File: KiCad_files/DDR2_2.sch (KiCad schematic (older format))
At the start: 16 parts, among them J6 EDY4016A

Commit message: Cleanup + Update to KiCad 5.0 + DDR2
Updated to KiCad 5, which re-organized libraries, so corrected them to not need RASAC-rescue.lib.
Also cleaned up some stuff.
DDR4 has been removed and in place will be DDR2.
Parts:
- removed J6: EDY4016A, symbol EDY4016A
- C101, C102, C103, C104, C105, C106, C107, C108, C109, C110, C111, C112: symbol C_Small -> Device:C_Small
- R29, R30: symbol R -> Device:R
- R31: symbol R_Small -> Device:R_Small
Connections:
- net labels added: DDR2_A0, DDR2_A1, DDR2_A10, DDR2_A11, DDR2_A12, DDR2_A13, DDR2_A14_WE_B, DDR2_A15_CAS_B, DDR2_A16_RAS_B, DDR2_A2, DDR2_A3, DDR2_A4, DDR2_A5, DDR2_A6, DDR2_A7, DDR2_A8, DDR2_A9, DDR2_ACT_N, DDR2_ALERT_N, DDR2_BA0, DDR2_BA1, DDR2_BG0, DDR2_CKE, DDR2_CK_C, DDR2_CK_T, DDR2_CS_N, DDR2_DM2, DDR2_DM3, DDR2_DQ16, DDR2_DQ17, DDR2_DQ18, DDR2_DQ19, DDR2_DQ20, DDR2_DQ21, DDR2_DQ22, DDR2_DQ23, DDR2_DQ24, DDR2_DQ25, DDR2_DQ26, DDR2_DQ27, DDR2_DQ28, DDR2_DQ29, DDR2_DQ30, DDR2_DQ31, DDR2_DQS2_C, DDR2_DQS2_T, DDR2_DQS3_C, DDR2_DQS3_T, DDR2_ODT, DDR2_PAR, DDR2_RESET_N, DDR2_TEN
- net labels removed: DDR4_A0, DDR4_A1, DDR4_A10, DDR4_A11, DDR4_A12, DDR4_A13, DDR4_A14_WE_B, DDR4_A15_CAS_B, DDR4_A16_RAS_B, DDR4_A2, DDR4_A3, DDR4_A4, DDR4_A5, DDR4_A6, DDR4_A7, DDR4_A8, DDR4_A9, DDR4_ACT_N, DDR4_ALERT_N, DDR4_BA0, DDR4_BA1, DDR4_BG0, DDR4_CKE, DDR4_CK_C, DDR4_CK_T, DDR4_CS_N, DDR4_DM2, DDR4_DM3, DDR4_DQ16, DDR4_DQ17, DDR4_DQ18, DDR4_DQ19, DDR4_DQ20, DDR4_DQ21, DDR4_DQ22, DDR4_DQ23, DDR4_DQ24, DDR4_DQ25, DDR4_DQ26, DDR4_DQ27, DDR4_DQ28, DDR4_DQ29, DDR4_DQ30, DDR4_DQ31, DDR4_DQS2_C, DDR4_DQS2_T, DDR4_DQS3_C, DDR4_DQS3_T, DDR4_ODT, DDR4_PAR, DDR4_RESET_N, DDR4_TEN
- wire segments 79 -> 135

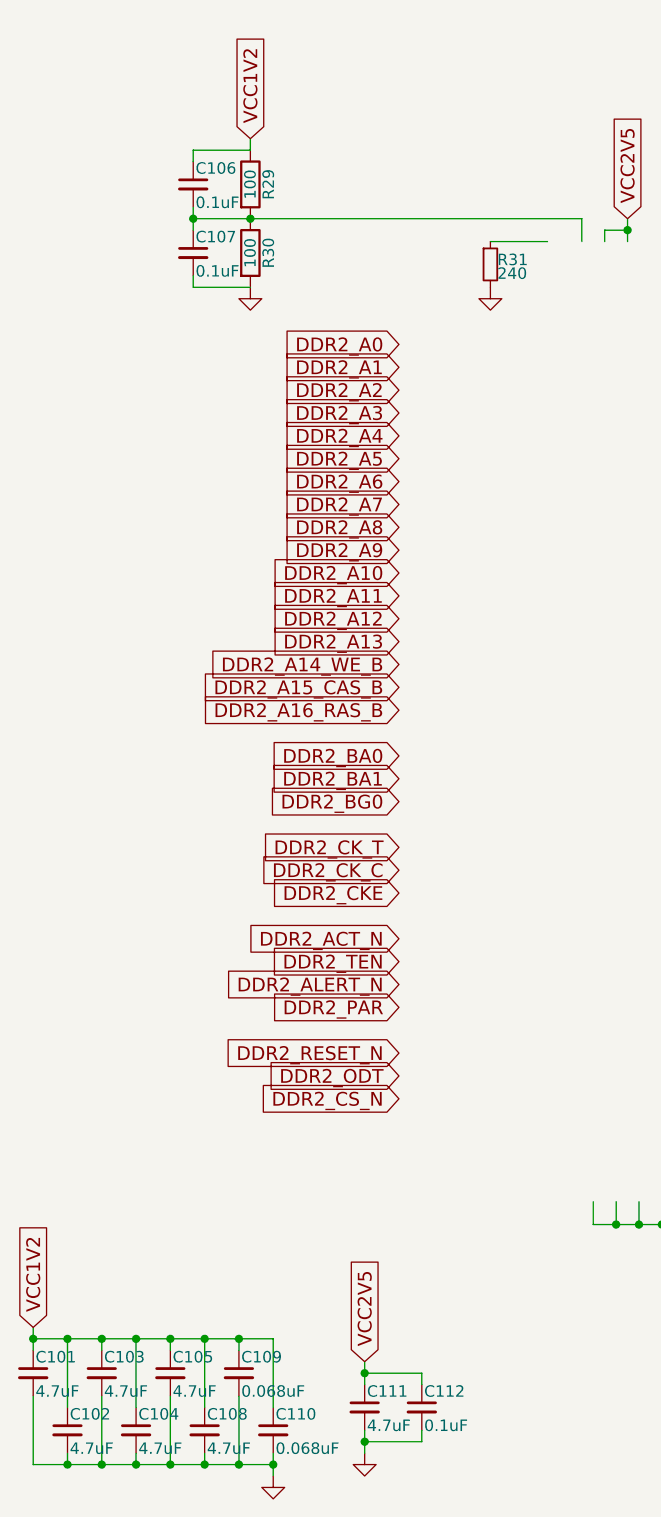
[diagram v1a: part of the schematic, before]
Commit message: Finished HDMI. Added I2C
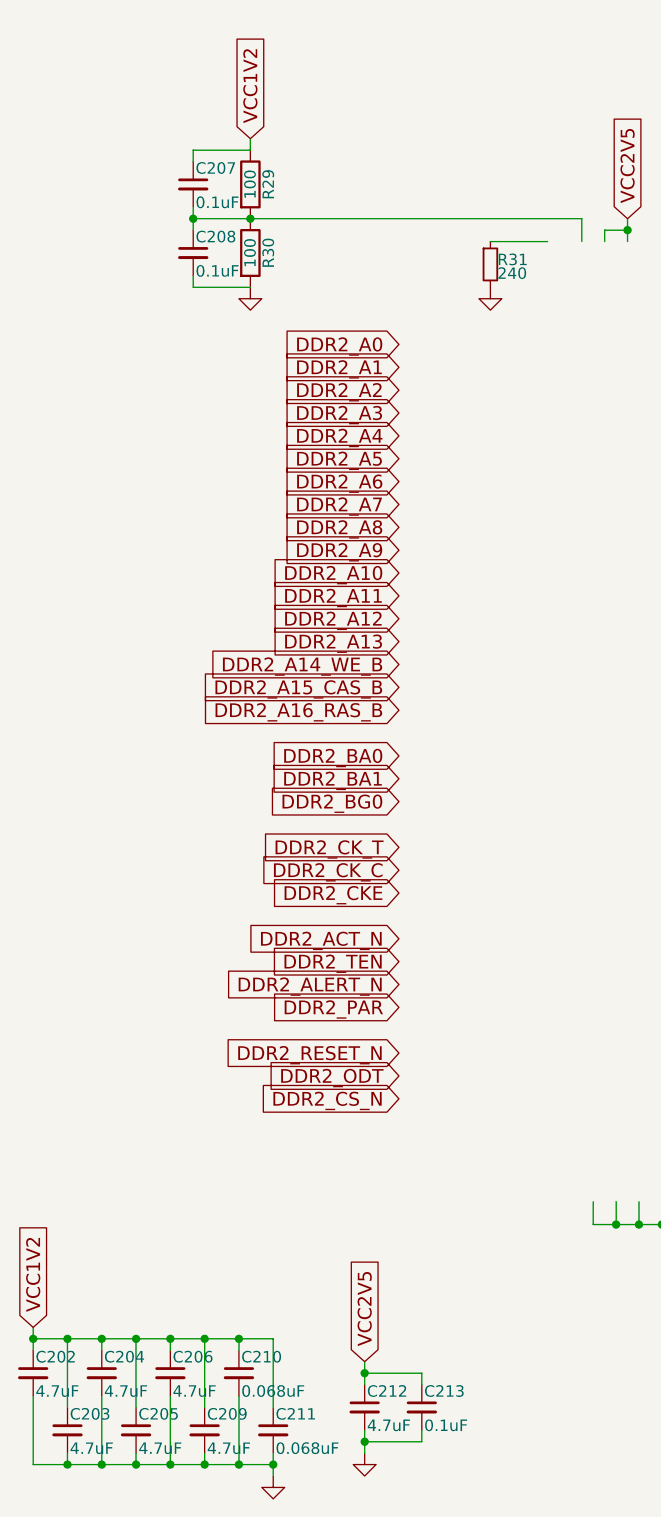
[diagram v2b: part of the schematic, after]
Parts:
- renumbered C101 to C202, C102 to C203, C103 to C204, C104 to C205, C105 to C206, C106 to C207, C107 to C208, C108 to C209, C109 to C210, C110 to C211, C111 to C212, C112 to C213
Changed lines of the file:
@@
 $EndComp
 $Comp
-L power:GND #PWR0102
+L power:GND #PWR0108
 U 1 1 5C14AF2F
 P 4550 2050
-F 0 "#PWR0102" H 4550 1800 50  0001 C CNN
+F 0 "#PWR0108" H 4550 1800 50  0001 C CNN
 F 1 "GND" H 4550 1900 50  0001 C CNN
 F 2 "" H 4550 2050 50  0001 C CNN
@@
 $EndComp
 $Comp
-L power:GND #PWR0103
+L power:GND #PWR0109
 U 1 1 5C14AF35
 P 6100 6250
-F 0 "#PWR0103" H 6100 6000 50  0001 C CNN
+F 0 "#PWR0109" H 6100 6000 50  0001 C CNN
 F 1 "GND" H 6100 6100 50  0001 C CNN
 F 2 "" H 6100 6250 50  0001 C CNN
@@
 $EndComp
 $Comp
-L power:GND #PWR099
+L power:GND #PWR0105
 U 1 1 5C14AF49
 P 3500 2050
-F 0 "#PWR099" H 3500 1800 50  0001 C CNN
+F 0 "#PWR0105" H 3500 1800 50  0001 C CNN
 F 1 "GND" H 3500 1900 50  0001 C CNN
 F 2 "" H 3500 2050 50  0001 C CNN
@@
 VCC1V2
 $Comp
-L Device:C_Small C107
+L Device:C_Small C208
 U 1 1 5C14AF50
 P 3250 1900
-F 0 "C107" H 3260 1970 50  0000 L CNN
+F 0 "C208" H 3260 1970 50  0000 L CNN
 F 1 "0.1uF" H 3260 1820 50  0000 L CNN
 F 2 "" H 3250 1900 50  0001 C CNN
@@
 $EndComp
 $Comp
-L Device:C_Small C106
+L Device:C_Small C207
 U 1 1 5C14AF57
 P 3250 1600
-F 0 "C106" H 3260 1670 50  0000 L CNN
+F 0 "C207" H 3260 1670 50  0000 L CNN
 F 1 "0.1uF" H 3260 1520 50  0000 L CNN
 F 2 "" H 3250 1600 50  0001 C CNN
@@
 VCC1V2
 $Comp
-L power:GND #PWR0100
+L power:GND #PWR0106
 U 1 1 5C14AF84
 P 3600 7250
-F 0 "#PWR0100" H 3600 7000 50  0001 C CNN
+F 0 "#PWR0106" H 3600 7000 50  0001 C CNN
 F 1 "GND" H 3600 7100 50  0001 C CNN
 F 2 "" H 3600 7250 50  0001 C CNN
@@
 $EndComp
 $Comp
-L Device:C_Small C101
+L Device:C_Small C202
 U 1 1 5C14AF8A
 P 2550 6800
-F 0 "C101" H 2560 6870 50  0000 L CNN
+F 0 "C202" H 2560 6870 50  0000 L CNN
 F 1 "4.7uF" H 2560 6720 50  0000 L CNN
 F 2 "" H 2550 6800 50  0001 C CNN
@@
 $EndComp
 $Comp
-L Device:C_Small C103
+L Device:C_Small C204
 U 1 1 5C14AF91
 P 2850 6800
-F 0 "C103" H 2860 6870 50  0000 L CNN
+F 0 "C204" H 2860 6870 50  0000 L CNN
 F 1 "4.7uF" H 2860 6720 50  0000 L CNN
 F 2 "" H 2850 6800 50  0001 C CNN
@@
 $EndComp
 $Comp
-L Device:C_Small C105
+L Device:C_Small C206
 U 1 1 5C14AF98
 P 3150 6800
-F 0 "C105" H 3160 6870 50  0000 L CNN
+F 0 "C206" H 3160 6870 50  0000 L CNN
 F 1 "4.7uF" H 3160 6720 50  0000 L CNN
 F 2 "" H 3150 6800 50  0001 C CNN
@@
 $EndComp
 $Comp
-L Device:C_Small C109
+L Device:C_Small C210
 U 1 1 5C14AF9F
 P 3450 6800
-F 0 "C109" H 3460 6870 50  0000 L CNN
+F 0 "C210" H 3460 6870 50  0000 L CNN
 F 1 "0.068uF" H 3460 6720 50  0000 L CNN
 F 2 "" H 3450 6800 50  0001 C CNN
@@
 $EndComp
 $Comp
-L Device:C_Small C102
+L Device:C_Small C203
 U 1 1 5C14AFA6
 P 2700 7050
-F 0 "C102" H 2710 7120 50  0000 L CNN
+F 0 "C203" H 2710 7120 50  0000 L CNN
 F 1 "4.7uF" H 2710 6970 50  0000 L CNN
 F 2 "" H 2700 7050 50  0001 C CNN
@@
 $EndComp
 $Comp
-L Device:C_Small C104
+L Device:C_Small C205
 U 1 1 5C14AFAD
 P 3000 7050
-F 0 "C104" H 3010 7120 50  0000 L CNN
+F 0 "C205" H 3010 7120 50  0000 L CNN
 F 1 "4.7uF" H 3010 6970 50  0000 L CNN
 F 2 "" H 3000 7050 50  0001 C CNN
@@
 $EndComp
 $Comp
-L Device:C_Small C108
+L Device:C_Small C209
 U 1 1 5C14AFB4
 P 3300 7050
-F 0 "C108" H 3310 7120 50  0000 L CNN
+F 0 "C209" H 3310 7120 50  0000 L CNN
 F 1 "4.7uF" H 3310 6970 50  0000 L CNN
 F 2 "" H 3300 7050 50  0001 C CNN
@@
 $EndComp
 $Comp
-L Device:C_Small C110
+L Device:C_Small C211
 U 1 1 5C14AFBB
 P 3600 7050
-F 0 "C110" H 3610 7120 50  0000 L CNN
+F 0 "C211" H 3610 7120 50  0000 L CNN
 F 1 "0.068uF" H 3610 6970 50  0000 L CNN
 F 2 "" H 3600 7050 50  0001 C CNN
@@
 Connection ~ 3450 7200
 $Comp
-L Device:C_Small C111
+L Device:C_Small C212
 U 1 1 5C14B041
 P 4000 6950
-F 0 "C111" H 4010 7020 50  0000 L CNN
+F 0 "C212" H 4010 7020 50  0000 L CNN
 F 1 "4.7uF" H 4010 6870 50  0000 L CNN
 F 2 "" H 4000 6950 50  0001 C CNN
@@
 $EndComp
 $Comp
-L power:GND #PWR0101
+L power:GND #PWR0107
 U 1 1 5C14B048
 P 4000 7150
-F 0 "#PWR0101" H 4000 6900 50  0001 C CNN
+F 0 "#PWR0107" H 4000 6900 50  0001 C CNN
 F 1 "GND" H 4000 7000 50  0001 C CNN
 F 2 "" H 4000 7150 50  0001 C CNN
@@
 $EndComp
 $Comp
-L Device:C_Small C112
+L Device:C_Small C213
 U 1 1 5C14B04E
 P 4250 6950
-F 0 "C112" H 4260 7020 50  0000 L CNN
+F 0 "C213" H 4260 7020 50  0000 L CNN
 F 1 "0.1uF" H 4260 6870 50  0000 L CNN
 F 2 "" H 4250 6950 50  0001 C CNN

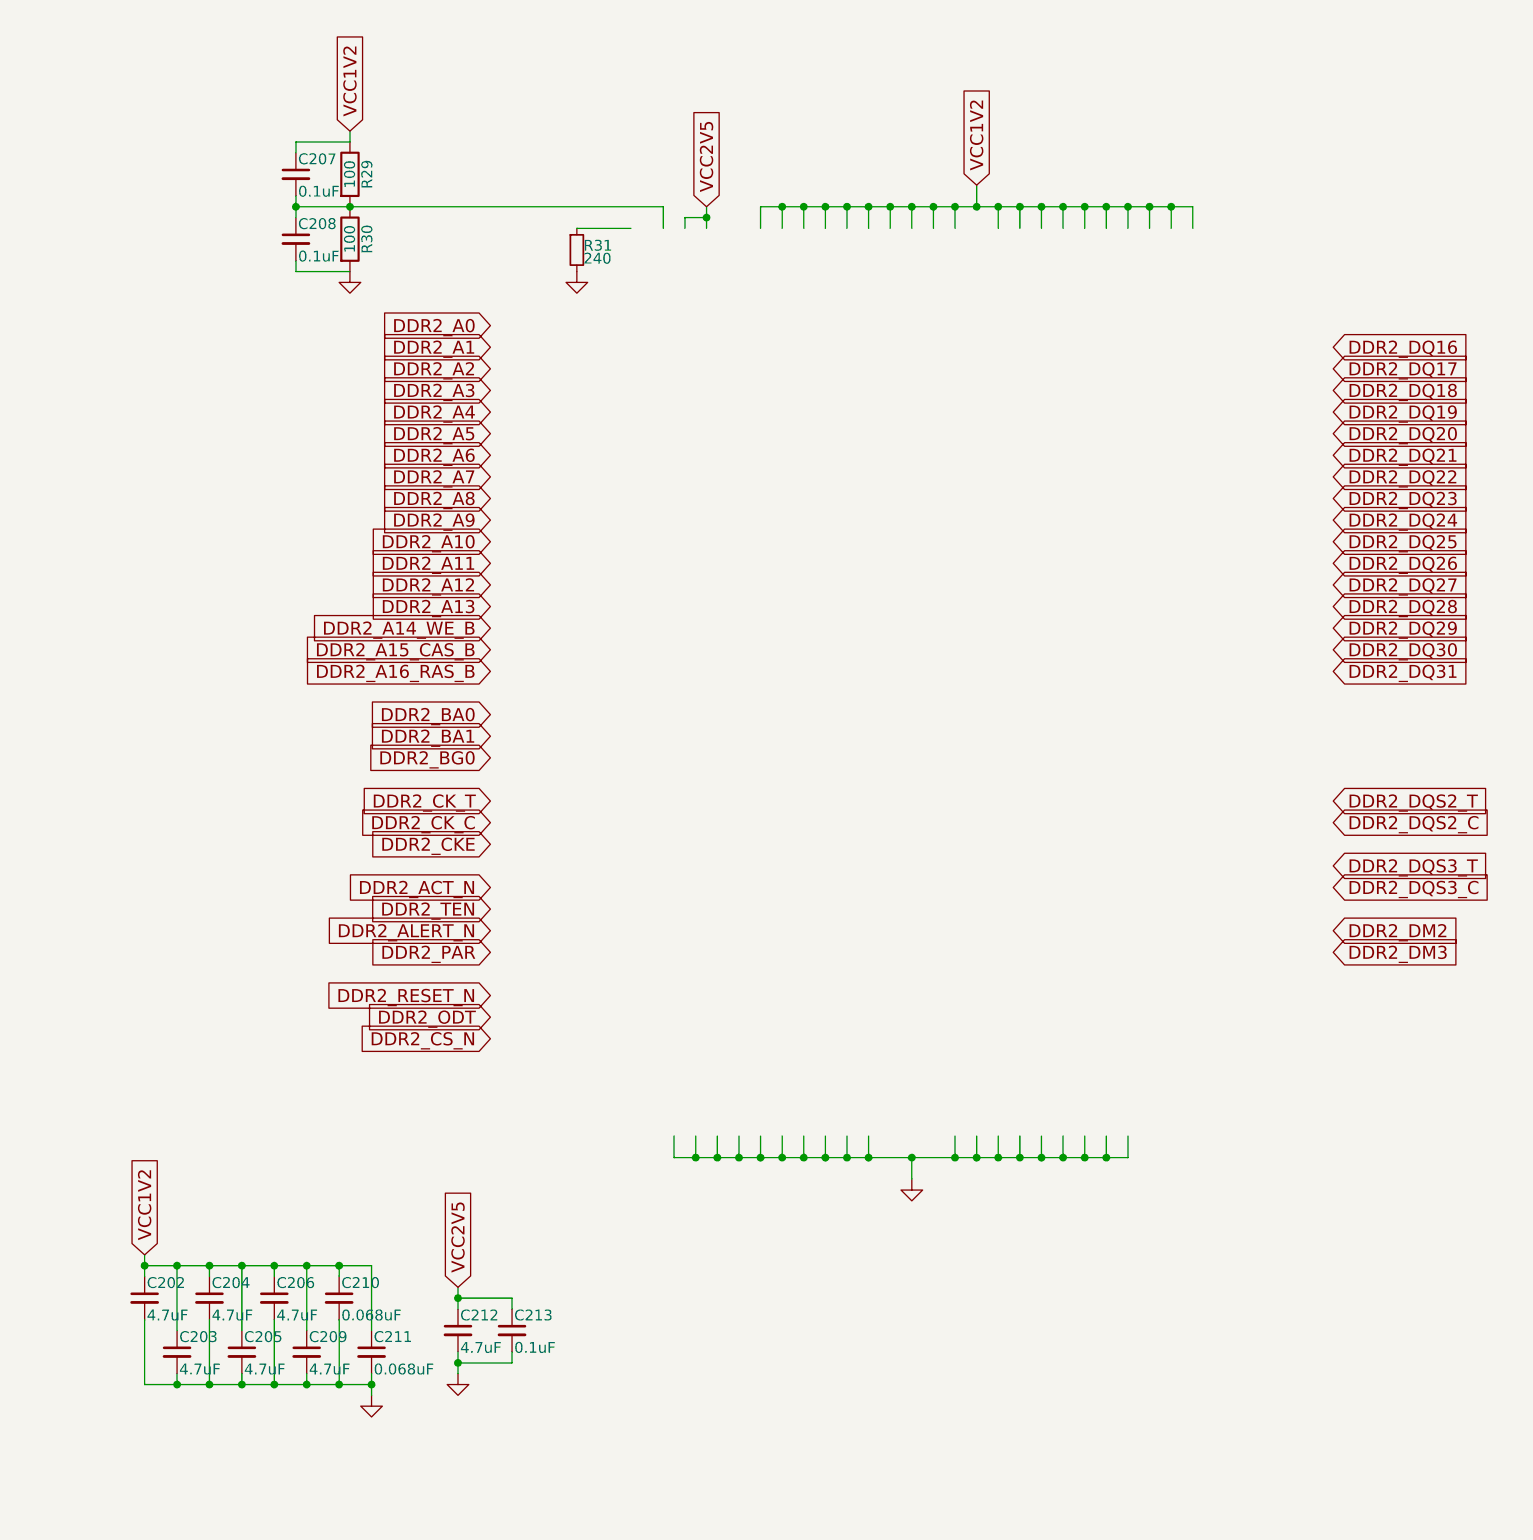
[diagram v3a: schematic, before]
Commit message: Cleanup for DRC and HDMI. HDMI and DDR2 looks good
DRC returns 5 errors with POWEROUTPUT-POWEROUTPUT set as good.
3 of them come from 3V3 since it's being driven from a MOSFET.
1 of them from VCC5V0 not yet supplied.
1 of them from USB_VBUS not set as output.
TODO:
5V supply for HDMI
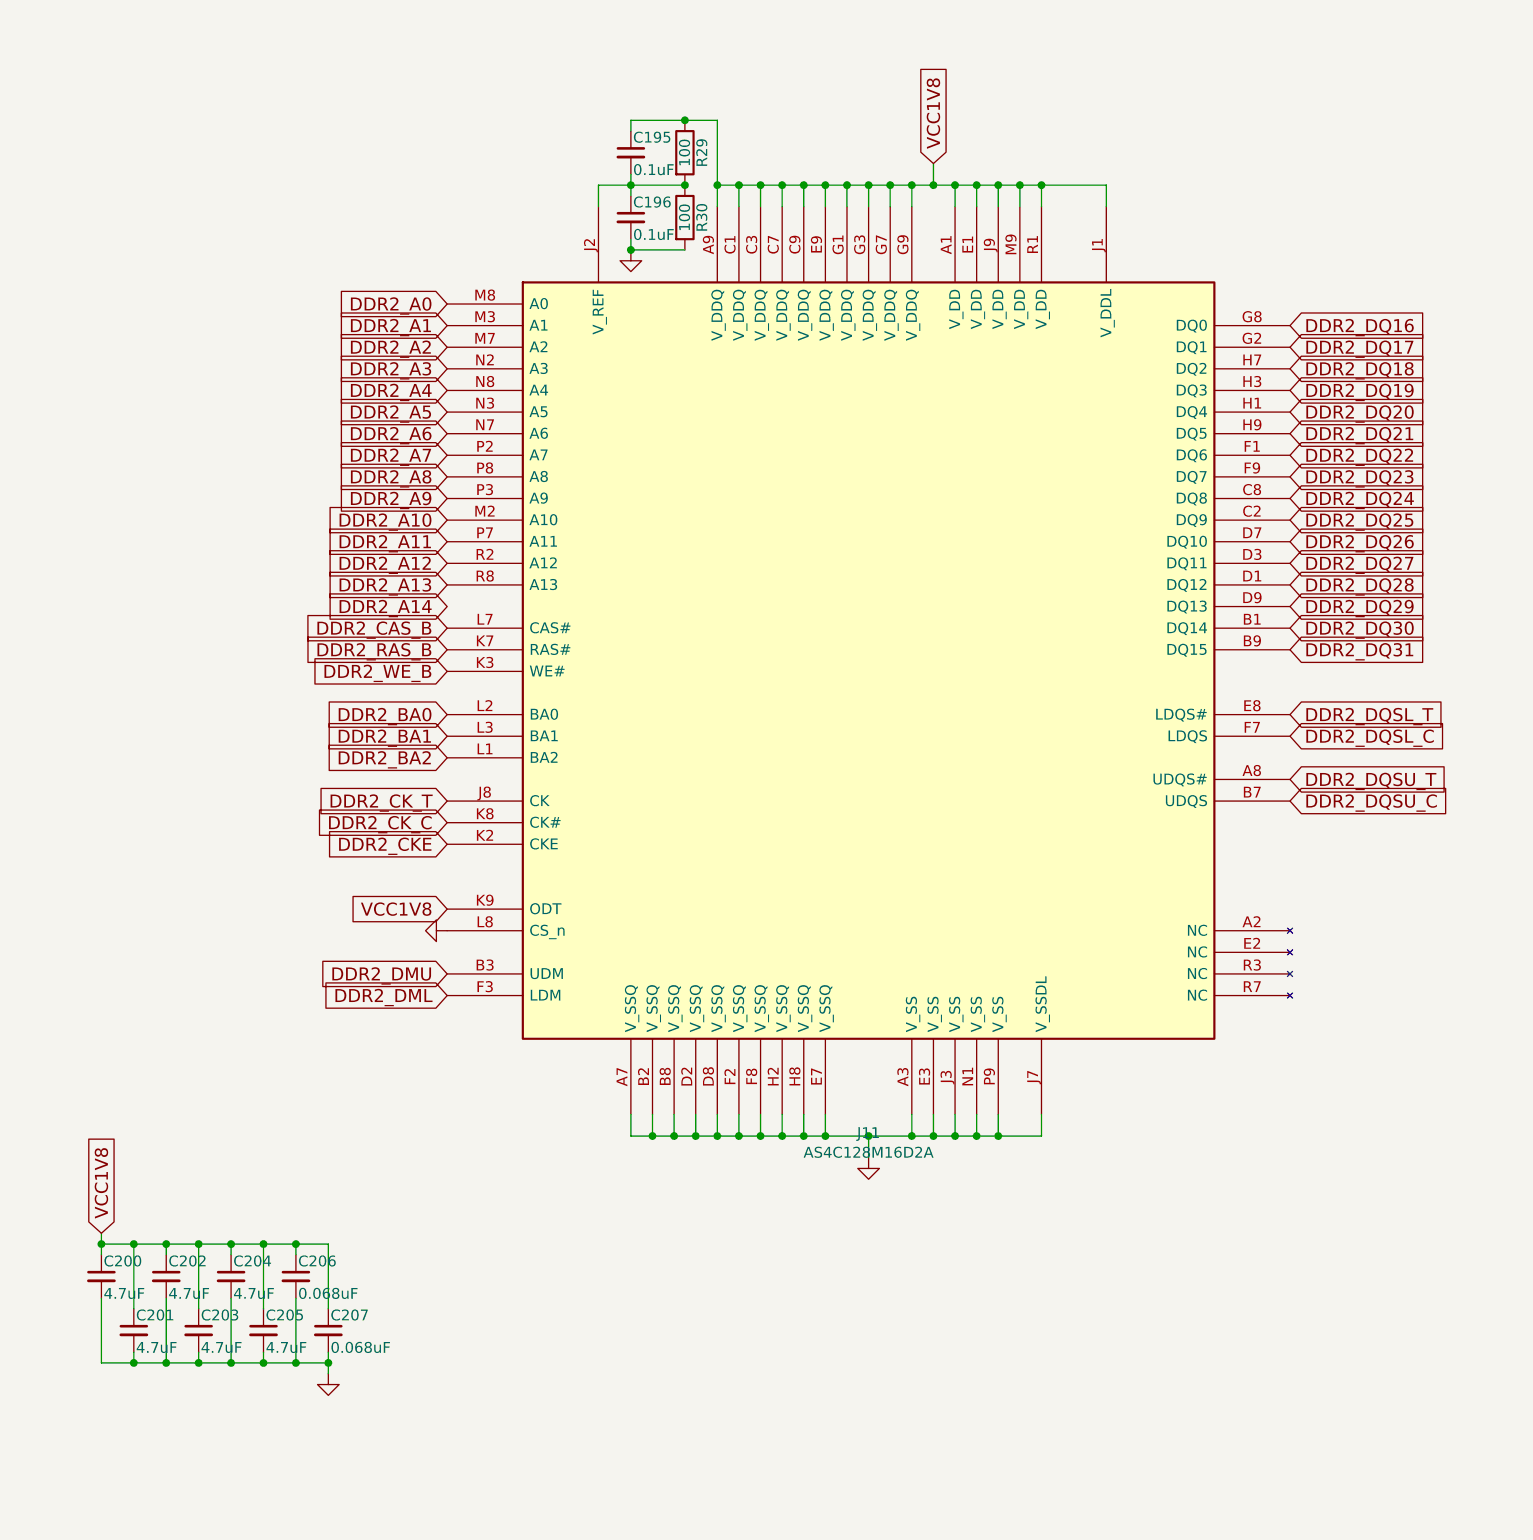
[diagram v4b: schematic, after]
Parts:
- removed C208, C213: 0.1uF, symbol Device:C_Small
- removed C209, C212: 4.7uF, symbol Device:C_Small
- removed C210, C211: 0.068uF, symbol Device:C_Small
- removed R31: 240, symbol Device:R_Small
- added C195, C196: 0.1uF, symbol Device:C_Small
- added C200, C201: 4.7uF, symbol Device:C_Small
- added J11: AS4C128M16D2A, symbol custom:AS4C128M16D2A
- C206: value 4.7uF -> 0.068uF
- C207: value 0.1uF -> 0.068uF
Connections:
- net labels added: DDR2_A14, DDR2_BA2, DDR2_CAS_B, DDR2_DML, DDR2_DMU, DDR2_DQSL_C, DDR2_DQSL_T, DDR2_DQSU_C, DDR2_DQSU_T, DDR2_RAS_B, DDR2_WE_B, VCC1V8
- net labels removed: DDR2_A14_WE_B, DDR2_A15_CAS_B, DDR2_A16_RAS_B, DDR2_ACT_N, DDR2_ALERT_N, DDR2_BG0, DDR2_CS_N, DDR2_DM2, DDR2_DM3, DDR2_DQS2_C, DDR2_DQS2_T, DDR2_DQS3_C, DDR2_DQS3_T, DDR2_ODT, DDR2_PAR, DDR2_RESET_N, DDR2_TEN, VCC1V2, VCC2V5
- wire segments 135 -> 109
